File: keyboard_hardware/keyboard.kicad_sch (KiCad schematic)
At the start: 17 parts, among them J1 USB_C_Receptacle_USB2.0_14P, J2 Conn_01x05, J3 Conn_01x15, J4 Conn_01x14, U2 LD3985M33R_SOT23, U3 USBLC6-2SC6

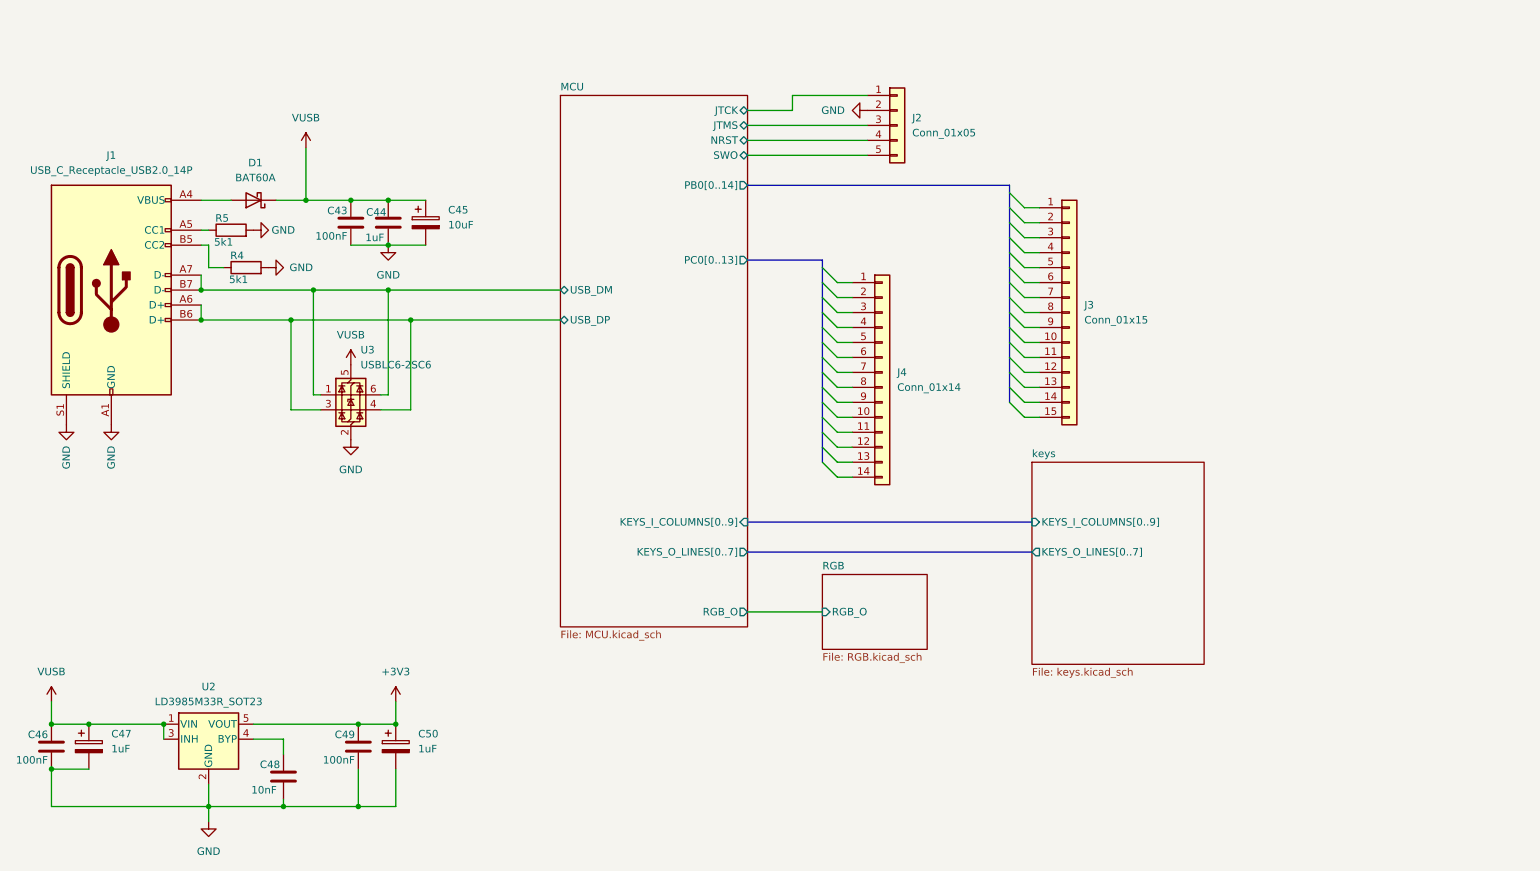
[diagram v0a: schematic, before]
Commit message: added rotary encoder
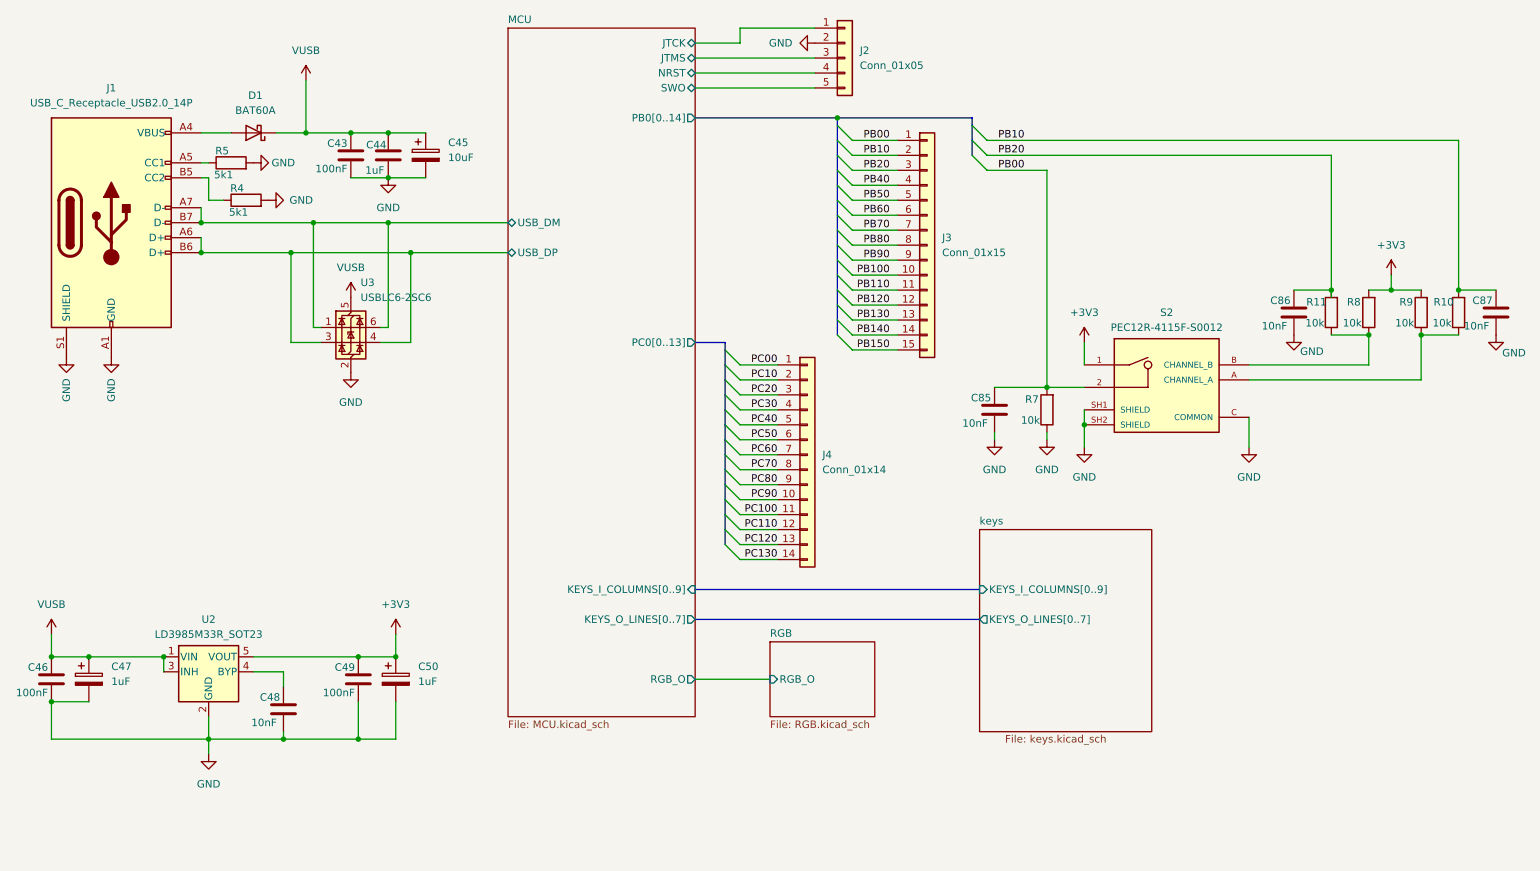
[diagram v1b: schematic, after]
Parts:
- added C85, C86, C87: 10nF, Capacitor_SMD:C_0603_1608Metric, symbol Device:C
- added R10, R11, R7, R8, R9: 10k, Resistor_SMD:R_0603_1608Metric, symbol Device:R
- added S2: PEC12R-4115F-S0012, PEC12R-4115F-S0012:XDCR_PEC12R-4115F-S0012, symbol meho1:PEC12R-4115F-S0012
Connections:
- net +3V3: now also R8.2, R9.2, S2.1
- net GND: now also C85.2, C86.2, C87.2, R7.1, S2.C (COMMON), S2.SH1 (SHIELD), S2.SH2 (SHIELD)
- net PB00: now reaches J3.1 (Pin_1)
- net PB00: now also C85.1, R7.2, S2.2
- net PB100: now reaches J3.10 (Pin_10)
- net PB110: now reaches J3.11 (Pin_11)
- net PB120: now reaches J3.12 (Pin_12)
- net PB130: now reaches J3.13 (Pin_13)
- net PB140: now reaches J3.14 (Pin_14)
- net PB150: now reaches J3.15 (Pin_15)
- net PB10: now reaches J3.2 (Pin_2)
- net PB10: now also C87.1, R10.2
- net PB20: now reaches J3.3 (Pin_3)
- net PB20: now also C86.1, R11.2
- net PB40: now reaches J3.4 (Pin_4)
- net PB50: now reaches J3.5 (Pin_5)
- net PB60: now reaches J3.6 (Pin_6)
- net PB70: now reaches J3.7 (Pin_7)
- net PB80: now reaches J3.8 (Pin_8)
- net PB90: now reaches J3.9 (Pin_9)
- net PC00: now reaches J4.1 (Pin_1)
- net PC90: now reaches J4.10 (Pin_10)
- net PC100: now reaches J4.11 (Pin_11)
- net PC110: now reaches J4.12 (Pin_12)
- net PC120: now reaches J4.13 (Pin_13)
- net PC130: now reaches J4.14 (Pin_14)
- net PC10: now reaches J4.2 (Pin_2)
- net PC20: now reaches J4.3 (Pin_3)
- net PC30: now reaches J4.4 (Pin_4)
- net PC40: now reaches J4.5 (Pin_5)
- net PC50: now reaches J4.6 (Pin_6)
- net PC60: now reaches J4.7 (Pin_7)
- net PC70: now reaches J4.8 (Pin_8)
- net PC80: now reaches J4.9 (Pin_9)
- new net: R11.1, R8.1, S2.B (CHANNEL_B)
- new net: R10.1, R9.1, S2.A (CHANNEL_A)
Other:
- moved on the sheet: C43, C44, C45, C46, C47, C48, C49, C50, D1, J1, J2, J3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
